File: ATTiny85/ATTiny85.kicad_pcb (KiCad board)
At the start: 2 copper layers, 18 x 24.3 mm, 28 parts, among them J2 Conn_01x05, J3 Conn_01x05, J4 ISP6, U1 ATtiny85-20SU

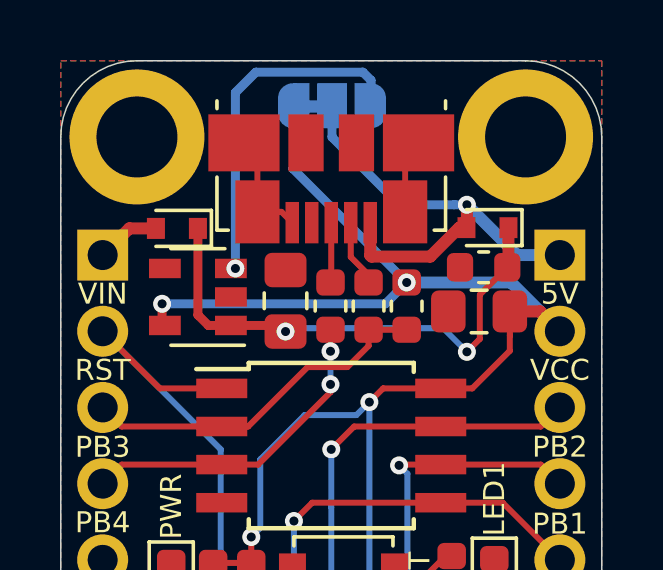
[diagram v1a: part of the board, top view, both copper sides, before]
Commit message: Spacings Updated
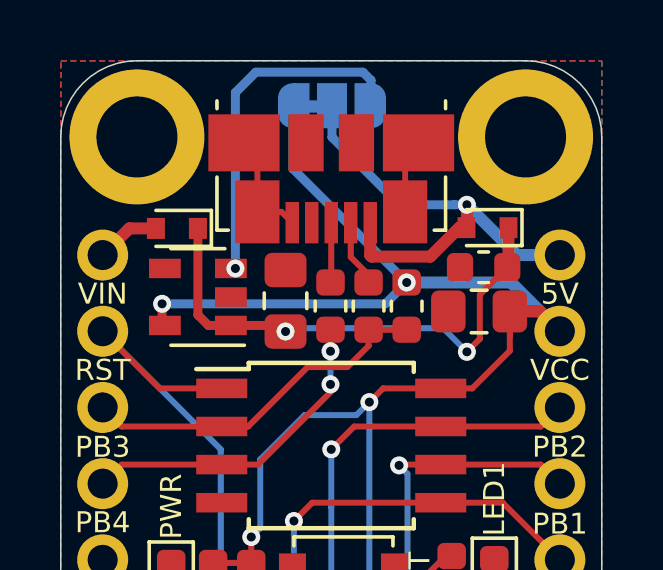
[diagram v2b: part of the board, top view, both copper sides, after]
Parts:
- J2, J3: moved to F.Cu
- turned J2 to 0 degrees
- turned J3 to 0 degrees
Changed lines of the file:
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@@
     (35 F.Paste user hide)
     (36 B.SilkS user)
-    (37 F.SilkS user hide)
+    (37 F.SilkS user)
     (38 B.Mask user)
     (39 F.Mask user hide)
@@
     (mod_text_size 1 1)
     (mod_text_width 0.15)
-    (pad_size 1.524 1.524)
-    (pad_drill 0.762)
+    (pad_size 1.7 1.7)
+    (pad_drill 1)
     (pad_to_mask_clearance 0.051)
     (solder_mask_min_width 0.25)
@@
     (add_net VCC)
     (add_net VIN)
+  )
+  (module Connector_PinHeader_2.54mm:PinHeader_1x05_P2.54mm_Vertical (layer F.Cu)
+    (at 177.1142 114.1476)
+    (descr "Through hole straight pin header, 1x05, 2.54mm pitch, single row")
+    (tags "Through hole pin header THT 1x05 2.54mm single row")
+    (fp_text reference J2 (at 0 -2.33 180) (layer F.SilkS) hide
+      (effects (font (size 1 1) (thickness 0.15)))
+    )
+    (fp_text value Conn_01x05 (at 0 12.49 180) (layer F.Fab)
+      (effects (font (size 1 1) (thickness 0.15)))
+    )
+    (fp_text user %R (at 0 5.08 -90) (layer F.Fab)
+      (effects (font (size 1 1) (thickness 0.15)))
+    )
+    (fp_line (start 1.8 -1.8) (end -1.8 -1.8) (layer F.CrtYd) (width 0.05))
+    (fp_line (start 1.8 11.95) (end 1.8 -1.8) (layer F.CrtYd) (width 0.05))
+    (fp_line (start -1.8 11.95) (end 1.8 11.95) (layer F.CrtYd) (width 0.05))
+    (fp_line (start -1.8 -1.8) (end -1.8 11.95) (layer F.CrtYd) (width 0.05))
+    (fp_line (start -1.27 -0.635) (end -0.635 -1.27) (layer F.Fab) (width 0.1))
+    (fp_line (start -1.27 11.43) (end -1.27 -0.635) (layer F.Fab) (width 0.1))
+    (fp_line (start 1.27 11.43) (end -1.27 11.43) (layer F.Fab) (width 0.1))
+    (fp_line (start 1.27 -1.27) (end 1.27 11.43) (layer F.Fab) (width 0.1))
+    (fp_line (start -0.635 -1.27) (end 1.27 -1.27) (layer F.Fab) (width 0.1))
+    (pad 5 thru_hole oval (at 0 10.16) (size 1.7 1.7) (drill 1) (layers *.Cu *.Mask)
+      (net 10 PB0))
+    (pad 4 thru_hole oval (at 0 7.62) (size 1.7 1.7) (drill 1) (layers *.Cu *.Mask)
+      (net 11 PB1))
+    (pad 3 thru_hole oval (at 0 5.08) (size 1.7 1.7) (drill 1) (layers *.Cu *.Mask)
+      (net 12 PB2))
+    (pad 2 thru_hole oval (at 0 2.54) (size 1.7 1.7) (drill 1) (layers *.Cu *.Mask)
+      (net 7 VCC))
+    (pad 1 thru_hole circle (at 0 0) (size 1.7 1.7) (drill 1) (layers *.Cu *.Mask)
+      (net 9 5V))
+    (model ${KISYS3DMOD}/Connector_PinHeader_2.54mm.3dshapes/PinHeader_1x05_P2.54mm_Vertical.wrl
+      (at (xyz 0 0 0))
+      (scale (xyz 1 1 1))
+      (rotate (xyz 0 0 0))
+    )
+  )
+  (module Connector_PinHeader_2.54mm:PinHeader_1x05_P2.54mm_Vertical (layer F.Cu)
+    (at 161.8742 114.1476)
+    (descr "Through hole straight pin header, 1x05, 2.54mm pitch, single row")
+    (tags "Through hole pin header THT 1x05 2.54mm single row")
+    (fp_text reference J3 (at 0 -2.33 180) (layer F.SilkS) hide
+      (effects (font (size 1 1) (thickness 0.15)))
+    )
+    (fp_text value Conn_01x05 (at 0 12.49 180) (layer F.Fab)
+      (effects (font (size 1 1) (thickness 0.15)))
+    )
+    (fp_text user %R (at 0 5.08 -90) (layer F.Fab)
+      (effects (font (size 1 1) (thickness 0.15)))
+    )
+    (fp_line (start 1.8 -1.8) (end -1.8 -1.8) (layer F.CrtYd) (width 0.05))
+    (fp_line (start 1.8 11.95) (end 1.8 -1.8) (layer F.CrtYd) (width 0.05))
+    (fp_line (start -1.8 11.95) (end 1.8 11.95) (layer F.CrtYd) (width 0.05))
+    (fp_line (start -1.8 -1.8) (end -1.8 11.95) (layer F.CrtYd) (width 0.05))
+    (fp_line (start -1.27 -0.635) (end -0.635 -1.27) (layer F.Fab) (width 0.1))
+    (fp_line (start -1.27 11.43) (end -1.27 -0.635) (layer F.Fab) (width 0.1))
+    (fp_line (start 1.27 11.43) (end -1.27 11.43) (layer F.Fab) (width 0.1))
+    (fp_line (start 1.27 -1.27) (end 1.27 11.43) (layer F.Fab) (width 0.1))
+    (fp_line (start -0.635 -1.27) (end 1.27 -1.27) (layer F.Fab) (width 0.1))
+    (pad 5 thru_hole oval (at 0 10.16) (size 1.7 1.7) (drill 1) (layers *.Cu *.Mask)
+      (net 13 GND))
+    (pad 4 thru_hole oval (at 0 7.62) (size 1.7 1.7) (drill 1) (layers *.Cu *.Mask)
+      (net 14 PB4))
+    (pad 3 thru_hole oval (at 0 5.08) (size 1.7 1.7) (drill 1) (layers *.Cu *.Mask)
+      (net 15 PB3))
+    (pad 2 thru_hole oval (at 0 2.54) (size 1.7 1.7) (drill 1) (layers *.Cu *.Mask)
+      (net 16 RST))
+    (pad 1 thru_hole circle (at 0 0) (size 1.7 1.7) (drill 1) (layers *.Cu *.Mask)
+      (net 8 VIN))
+    (model ${KISYS3DMOD}/Connector_PinHeader_2.54mm.3dshapes/PinHeader_1x05_P2.54mm_Vertical.wrl
+      (at (xyz 0 0 0))
+      (scale (xyz 1 1 1))
+      (rotate (xyz 0 0 0))
+    )
   )
   (module logo:SirBoard98x31 (layer B.Cu)
@@
       (at (xyz 0 0 0))
       (scale (xyz 1 1 1))
-      (rotate (xyz 0 0 0))
-    )
-  )
-  (module Connector_PinHeader_2.54mm:PinHeader_1x05_P2.54mm_Vertical (layer B.Cu)
-    (at 161.8742 114.1476 180)
-    (descr "Through hole straight pin header, 1x05, 2.54mm pitch, single row")
-    (tags "Through hole pin header THT 1x05 2.54mm single row")
-    (fp_text reference J3 (at 0 2.33) (layer B.SilkS) hide
-      (effects (font (size 1 1) (thickness 0.15)) (justify mirror))
-    )
-    (fp_text value Conn_01x05 (at 0 -12.49) (layer B.Fab)
-      (effects (font (size 1 1) (thickness 0.15)) (justify mirror))
-    )
-    (fp_text user %R (at 0 -5.08 270) (layer B.Fab)
-      (effects (font (size 1 1) (thickness 0.15)) (justify mirror))
-    )
-    (fp_line (start 1.8 1.8) (end -1.8 1.8) (layer B.CrtYd) (width 0.05))
-    (fp_line (start 1.8 -11.95) (end 1.8 1.8) (layer B.CrtYd) (width 0.05))
-    (fp_line (start -1.8 -11.95) (end 1.8 -11.95) (layer B.CrtYd) (width 0.05))
-    (fp_line (start -1.8 1.8) (end -1.8 -11.95) (layer B.CrtYd) (width 0.05))
-    (fp_line (start -1.33 1.33) (end 0 1.33) (layer B.SilkS) (width 0.12))
-    (fp_line (start -1.33 0) (end -1.33 1.33) (layer B.SilkS) (width 0.12))
-    (fp_line (start -1.33 -1.27) (end 1.33 -1.27) (layer B.SilkS) (width 0.12))
-    (fp_line (start 1.33 -1.27) (end 1.33 -11.49) (layer B.SilkS) (width 0.12))
-    (fp_line (start -1.33 -1.27) (end -1.33 -11.49) (layer B.SilkS) (width 0.12))
-    (fp_line (start -1.33 -11.49) (end 1.33 -11.49) (layer B.SilkS) (width 0.12))
-    (fp_line (start -1.27 0.635) (end -0.635 1.27) (layer B.Fab) (width 0.1))
-    (fp_line (start -1.27 -11.43) (end -1.27 0.635) (layer B.Fab) (width 0.1))
-    (fp_line (start 1.27 -11.43) (end -1.27 -11.43) (layer B.Fab) (width 0.1))
-    (fp_line (start 1.27 1.27) (end 1.27 -11.43) (layer B.Fab) (width 0.1))
-    (fp_line (start -0.635 1.27) (end 1.27 1.27) (layer B.Fab) (width 0.1))
-    (pad 5 thru_hole oval (at 0 -10.16 180) (size 1.7 1.7) (drill 1) (layers *.Cu *.Mask)
-      (net 13 GND))
-    (pad 4 thru_hole oval (at 0 -7.62 180) (size 1.7 1.7) (drill 1) (layers *.Cu *.Mask)
-      (net 14 PB4))
-    (pad 3 thru_hole oval (at 0 -5.08 180) (size 1.7 1.7) (drill 1) (layers *.Cu *.Mask)
-      (net 15 PB3))
-    (pad 2 thru_hole oval (at 0 -2.54 180) (size 1.7 1.7) (drill 1) (layers *.Cu *.Mask)
-      (net 16 RST))
-    (pad 1 thru_hole rect (at 0 0 180) (size 1.7 1.7) (drill 1) (layers *.Cu *.Mask)
-      (net 8 VIN))
-    (model ${KISYS3DMOD}/Connector_PinHeader_2.54mm.3dshapes/PinHeader_1x05_P2.54mm_Vertical.wrl
-      (at (xyz 0 0 0))
-      (scale (xyz 1 1 1))
-      (rotate (xyz 0 0 0))
-    )
-  )
-  (module Connector_PinHeader_2.54mm:PinHeader_1x05_P2.54mm_Vertical (layer B.Cu)
-    (at 177.1142 114.1476 180)
-    (descr "Through hole straight pin header, 1x05, 2.54mm pitch, single row")
-    (tags "Through hole pin header THT 1x05 2.54mm single row")
-    (fp_text reference J2 (at 0 2.33) (layer B.SilkS) hide
-      (effects (font (size 1 1) (thickness 0.15)) (justify mirror))
-    )
-    (fp_text value Conn_01x05 (at 0 -12.49) (layer B.Fab)
-      (effects (font (size 1 1) (thickness 0.15)) (justify mirror))
-    )
-    (fp_text user %R (at 0 -5.08 270) (layer B.Fab)
-      (effects (font (size 1 1) (thickness 0.15)) (justify mirror))
-    )
-    (fp_line (start 1.8 1.8) (end -1.8 1.8) (layer B.CrtYd) (width 0.05))
-    (fp_line (start 1.8 -11.95) (end 1.8 1.8) (layer B.CrtYd) (width 0.05))
-    (fp_line (start -1.8 -11.95) (end 1.8 -11.95) (layer B.CrtYd) (width 0.05))
-    (fp_line (start -1.8 1.8) (end -1.8 -11.95) (layer B.CrtYd) (width 0.05))
-    (fp_line (start -1.33 1.33) (end 0 1.33) (layer B.SilkS) (width 0.12))
-    (fp_line (start -1.33 0) (end -1.33 1.33) (layer B.SilkS) (width 0.12))
-    (fp_line (start -1.33 -1.27) (end 1.33 -1.27) (layer B.SilkS) (width 0.12))
-    (fp_line (start 1.33 -1.27) (end 1.33 -11.49) (layer B.SilkS) (width 0.12))
-    (fp_line (start -1.33 -1.27) (end -1.33 -11.49) (layer B.SilkS) (width 0.12))
-    (fp_line (start -1.33 -11.49) (end 1.33 -11.49) (layer B.SilkS) (width 0.12))
-    (fp_line (start -1.27 0.635) (end -0.635 1.27) (layer B.Fab) (width 0.1))
-    (fp_line (start -1.27 -11.43) (end -1.27 0.635) (layer B.Fab) (width 0.1))
-    (fp_line (start 1.27 -11.43) (end -1.27 -11.43) (layer B.Fab) (width 0.1))
-    (fp_line (start 1.27 1.27) (end 1.27 -11.43) (layer B.Fab) (width 0.1))
-    (fp_line (start -0.635 1.27) (end 1.27 1.27) (layer B.Fab) (width 0.1))
-    (pad 5 thru_hole oval (at 0 -10.16 180) (size 1.7 1.7) (drill 1) (layers *.Cu *.Mask)
-      (net 10 PB0))
-    (pad 4 thru_hole oval (at 0 -7.62 180) (size 1.7 1.7) (drill 1) (layers *.Cu *.Mask)
-      (net 11 PB1))
-    (pad 3 thru_hole oval (at 0 -5.08 180) (size 1.7 1.7) (drill 1) (layers *.Cu *.Mask)
-      (net 12 PB2))
-    (pad 2 thru_hole oval (at 0 -2.54 180) (size 1.7 1.7) (drill 1) (layers *.Cu *.Mask)
-      (net 7 VCC))
-    (pad 1 thru_hole rect (at 0 0 180) (size 1.7 1.7) (drill 1) (layers *.Cu *.Mask)
-      (net 9 5V))
-    (model ${KISYS3DMOD}/Connector_PinHeader_2.54mm.3dshapes/PinHeader_1x05_P2.54mm_Vertical.wrl
-      (at (xyz 0 0 0))
-      (scale (xyz 1 1 1))

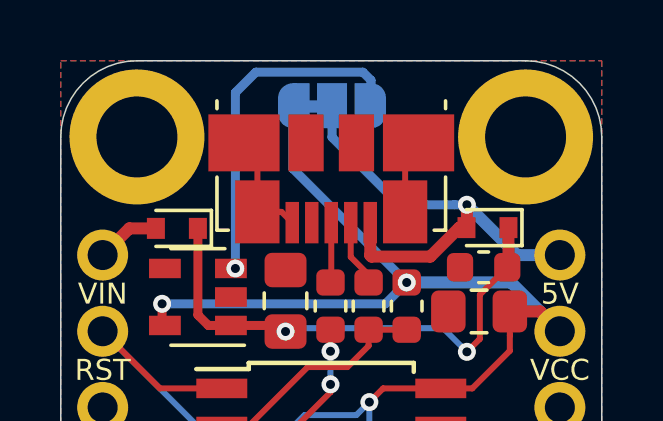
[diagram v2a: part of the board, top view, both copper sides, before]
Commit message: Silkscreens Orientated
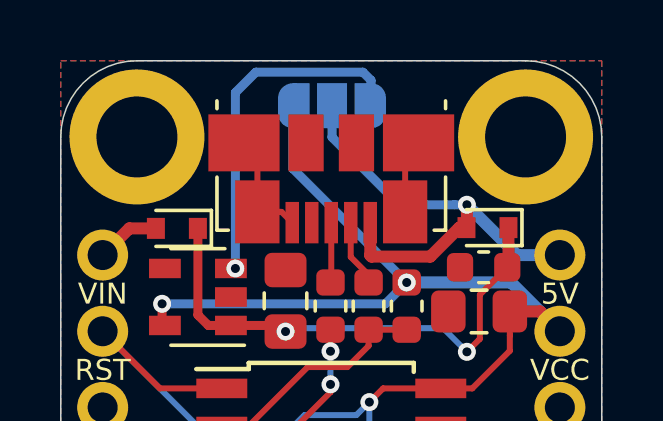
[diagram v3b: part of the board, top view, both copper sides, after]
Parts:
- 3.3V       5V: footprint Jumper:SolderJumper-3_P1.3mm_Bridged12_RoundedPad1.0x1.5mm -> Jumper:SolderJumper-3_P1.3mm_Open_RoundedPad1.0x1.5mm
- J2, J3: moved to B.Cu
- turned J2 to 180 degrees
- turned J3 to 180 degrees

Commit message: Schematic PDF and 3D Renders added
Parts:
- removed PS1: 1, Package_TO_SOT_SMD:SOT-23-5
- added U2: AP2127K-3.3, Package_TO_SOT_SMD:SOT-23-5, F.Cu at (61.4, 33.3)
- LED1: value SFH460 -> Blue
- PWR: value SFH460 -> Red
- R5: value 33k -> 10K
- moved 3.3V       5V 132.3 mm to (65.8, 26.9)
- moved J2 132.3 mm to (73.4, 31.9)
- moved PWR 132.3 mm to (60.5, 43.0)
- moved R5 132.3 mm to (63.1, 43.0)
- moved R8 132.3 mm to (68.3, 33.6)
- moved REF** 132.3 mm to (72.3, 47.2)
- moved REF** 132.3 mm to (72.3, 28.0)
- moved U1 132.3 mm to (65.8, 38.3)
- moved USB1 132.3 mm to (65.8, 29.4)
- moved C1 132.3 mm to (70.9, 32.3)
- moved C3 132.3 mm to (64.3, 33.5)
- moved C4 132.3 mm to (70.7, 33.8)
- moved D1 132.3 mm to (60.7, 31.0)
- moved D2 132.3 mm to (71.0, 31.0)
- moved G*** 132.3 mm to (66.0, 41.7)
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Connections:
- net 5V renamed VUSB
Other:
- rule pad_to_mask_clearance: 0.051 -> 0
- rule solder_mask_min_width: 0.25 -> 0.1

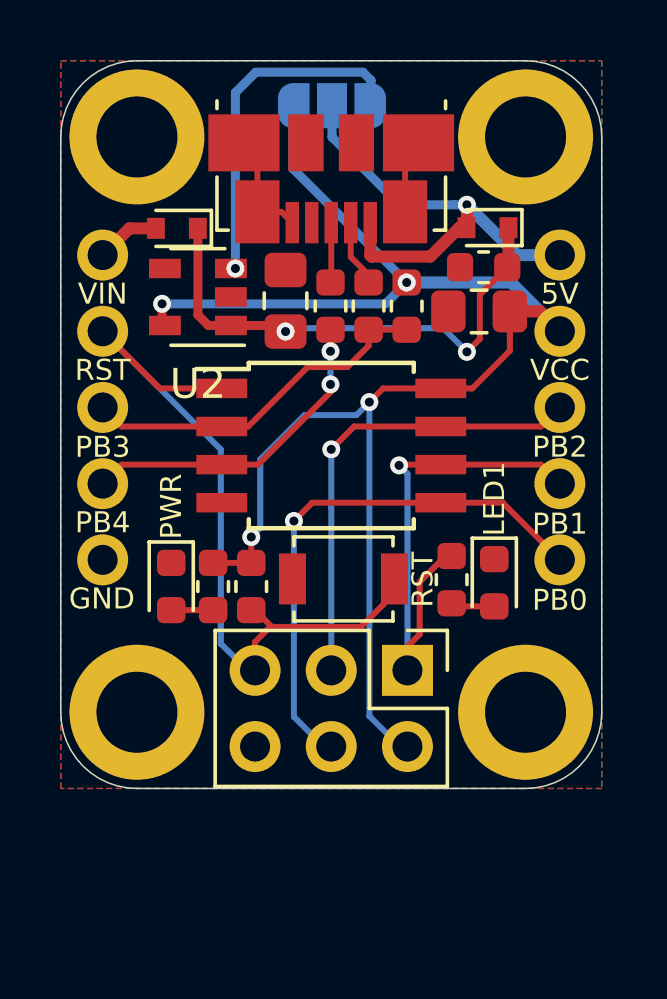
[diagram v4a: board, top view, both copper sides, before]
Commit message: ATTiny85 Revision 2
USB-C, SPX3819, QFN Package and Board Size Revision
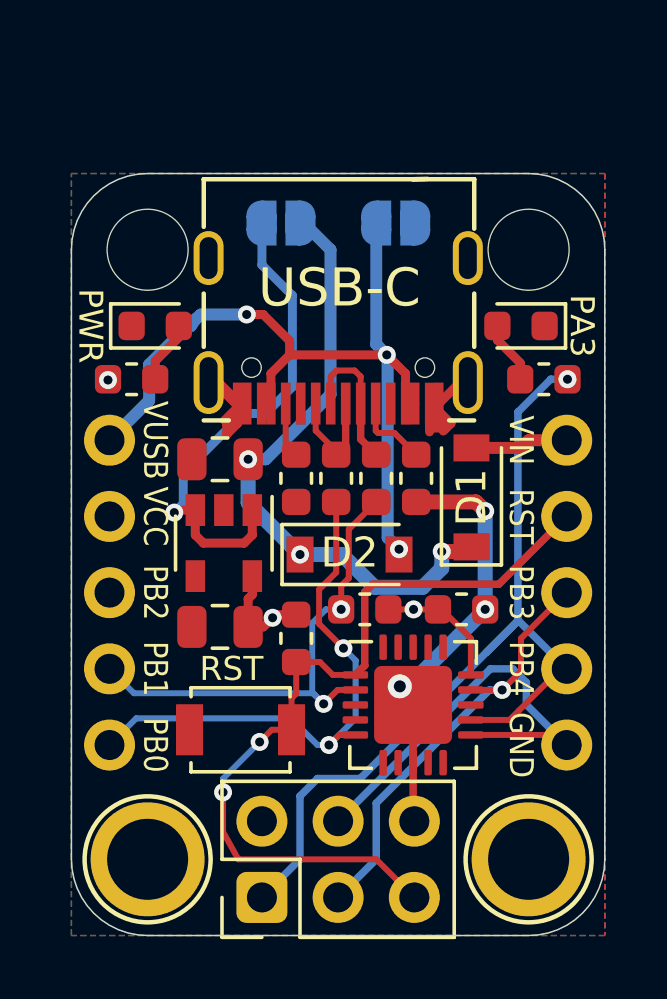
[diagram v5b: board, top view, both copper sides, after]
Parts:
- removed 3.3V       5V: SolderJumper_3_Bridged12, Jumper:SolderJumper-3_P1.3mm_Open_RoundedPad1.0x1.5mm
- removed C4: 10uF, Capacitor_SMD:C_0805_2012Metric_Pad1.15x1.40mm_HandSolder
- removed the G*** at (66.0, 41.7)
- removed the G*** at (65.9, 36.8)
- removed the G*** at (65.8, 29.4)
- removed LED1: Blue, LED_SMD:LED_0603_1608Metric
- removed R9: 68e, Resistor_SMD:R_0603_1608Metric
- removed REF** (x4): MountingHole_2.7mm_M2.5_ISO7380_Pad, MountingHole:MountingHole_2.7mm_M2.5_ISO7380_Pad
- removed USB1: USB_B_Micro, Connector_USB:USB_Micro-B_Molex_47346-0001
- added 3V3: SolderJumper_2_Open, Jumper:SolderJumper-2_P1.3mm_Open_RoundedPad1.0x1.5mm, B.Cu at (64.1, 30.9)
- added 5V: SolderJumper_2_Open, Jumper:SolderJumper-2_P1.3mm_Open_RoundedPad1.0x1.5mm, B.Cu at (68.0, 30.9)
- added C2: 10uF, Capacitor_SMD:C_0805_2012Metric, F.Cu at (62.1, 44.3)
- added G***: LOGO, logo:SirBoard127x40, B.Cu at (66.0, 43.4)
- added G***: LOGO, logo:logo76x107, B.Cu at (66.0, 37.1)
- added H1: MountingHole, MountingHole:MountingHole_2.7mm_M2.5, F.Cu at (59.7, 31.8)
- added H2: MountingHole, SirBoardLibrary:MountingHole_M2.5_SirBoard, F.Cu at (72.4, 52.1)
- added H3: MountingHole, SirBoardLibrary:MountingHole_M2.5_SirBoard, F.Cu at (59.7, 52.1)
- added H4: MountingHole, MountingHole:MountingHole_2.7mm_M2.5, F.Cu at (72.4, 31.8)
- added PA3: RED, LED_SMD:LED_0603_1608Metric, F.Cu at (72.1, 34.3)
- added R1: 5k1, Resistor_SMD:R_0603_1608Metric, F.Cu at (64.6, 39.4)
- added R2: 5k1, Resistor_SMD:R_0603_1608Metric, F.Cu at (68.6, 39.4)
- added R3: 68e, Resistor_SMD:R_0603_1608Metric, F.Cu at (67.3, 39.4)
- added USB-C: USB_C_Receptacle_USB2.0, SirBoardLibrary:USB_C, F.Cu at (69.3, 37.5)
- C1: value 1uF -> 10uF; footprint Capacitor_SMD:C_0603_1608Metric -> Capacitor_SMD:C_0805_2012Metric
- C3: value 10uF -> 100nF; footprint Capacitor_SMD:C_0805_2012Metric_Pad1.15x1.40mm_HandSolder -> Capacitor_SMD:C_0603_1608Metric
- D1, D2: value 1N4148WT -> MBR120; footprint Diode_SMD:D_SOD-523 -> Diode_SMD:D_SOD-123
- PWR: value Red -> RED
- R4: value 1k -> 68e
- R6: value 68e -> 1k5
- R7: value 1k -> 1K
- R8: value 1k5 -> 1K
- U1: value ATtiny85-20SU -> ATtiny85-20MU; footprint Package_SO:SOIJ-8_5.3x5.3mm_P1.27mm -> Package_DFN_QFN:QFN-20-1EP_4x4mm_P0.5mm_EP2.6x2.6mm
- U2: value AP2127K-3.3 -> SPX3819M5-L-3-3
- moved J3 16.7 mm to (73.7, 38.1)
- moved J2 16.2 mm to (58.4, 38.1)
- moved D1 13.3 mm to (70.5, 40.0), turned to 90 degrees
- moved C3 11.8 mm to (70.2, 43.7), turned to 0 degrees
- moved D2 11.8 mm to (66.4, 41.9), turned to 0 degrees
- moved C1 10.9 mm to (62.1, 38.7)
- moved R6 10.2 mm to (66.9, 43.7), turned to 0 degrees
- moved R8 9.49 mm to (59.2, 36.1), turned to 180 degrees
- moved U1 9.07 mm to (68.5, 46.9)
- moved J4 8.99 mm to (63.5, 53.3), turned to 90 degrees
- moved PWR 8.70 mm to (59.9, 34.3), turned to 0 degrees
- moved U2 8.25 mm to (62.2, 41.5), turned to 270 degrees
- moved R7 7.35 mm to (72.9, 36.1), turned to 0 degrees
- moved RST 6.09 mm to (62.8, 47.8)
- moved R4 5.46 mm to (66.0, 39.4)
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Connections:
- C1 pad 1: Net-(C1-Pad1) -> Net-(3V3-Pad1)
- C3 pad 1: Net-(C1-Pad1) -> VCC
- D1 pad 1: Net-(C1-Pad1) -> Net-(3V3-Pad1)
- D2 pad 1: Net-(C1-Pad1) -> Net-(3V3-Pad1)
- J2 pad 3: PB2 -> GND
- J2 pad 4: PB1 -> PB3
- J2 pad 5: PB0 -> PB4
- J3 pad 3: PB3 -> PB2
- J3 pad 4: PB4 -> PB1
- J3 pad 5: GND -> PB0
- PWR pad 2: Net-(PWR1-Pad2) -> Net-(D4-Pad2)
- R4 pad 1: VCC -> Net-(J1-PadA6)
- R4 pad 2: Net-(PWR1-Pad2) -> PB4
- R6 pad 1: Net-(R6-Pad1) -> PB3
- R6 pad 2: PB4 -> VCC
- R7 pad 1: PB1 -> Net-(D3-Pad2)
- R7 pad 2: Net-(LED1-Pad2) -> PB1
- R8 pad 1: PB3 -> Net-(D4-Pad2)
- U1 pad 3: PB4 -> Net-(U1-Pad3)
- U1 pad 4: GND -> Net-(U1-Pad4)
- U1 pad 5: PB0 -> PB4
- U1 pad 6: PB1 -> Net-(U1-Pad6)
- U1 pad 7: PB2 -> Net-(U1-Pad7)
- U1 pad 8: VCC -> GND
- U2 pad 1: Net-(C1-Pad1) -> Net-(3V3-Pad2)
- U2 pad 3: Net-(JP1-Pad3) -> Net-(3V3-Pad2)
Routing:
- net VCC: track 52.6 -> 8.07 mm, vias 4 -> 3
- net Net-(3V3-Pad1): track 0.00 -> 20.7 mm, vias 0 -> 3
- net GND: track 6.28 -> 23.8 mm, vias 0 -> 3
- net Net-(C1-Pad1): track 17.2 -> 0.00 mm, vias 2 -> 0
- net Net-(3V3-Pad2): track 0.00 -> 16.5 mm, vias 0 -> 1
- net PB1: track 17.4 -> 30.3 mm
- net VUSB: track 15.8 -> 28.1 mm, vias 1 -> 3
- net Net-(JP1-Pad3): track 11.6 -> 0.00 mm, vias 1 -> 0
- net PB4: track 10.9 -> 18.3 mm
- net PB3: track 12.0 -> 16.9 mm, vias 0 -> 2
- net Net-(J1-PadA7): track 0.00 -> 4.89 mm
- net Net-(J1-PadA6): track 0.00 -> 3.82 mm
- net PB0: track 18.2 -> 14.5 mm, vias 1 -> 0
- net Net-(J1-PadA5): track 0.00 -> 2.58 mm
- net Net-(R9-Pad2): track 2.24 -> 0.00 mm
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- added copper zone on B.Cu, net VCC
- removed copper zone on B.Cu, net GND
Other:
- board size 18 x 24.3 mm -> 17.8 x 25.4 mm
- board text added: "ATTiny85 Dev Board With 3V3 and 5V"
- board text added: "VUSB"
- board text removed: "5V"
- board text removed: "Development Board for the ATTiny85"
